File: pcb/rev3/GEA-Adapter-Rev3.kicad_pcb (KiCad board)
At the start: 2 copper layers, 88.7 x 40 mm, 109 parts, among them J1 8P8C, J3 TC2030, J4 USB_C_Receptacle_USB2.0_16P, Q3 CJ3407, Q4 CJ3407, Q5 MMBT3904, SW1 SW_Push, SW2 SW_Push, U10 TPS22810DBVR, U2 ESP32-C3-WROOM-02, U4 74LVC2G07, U5 74LVC2G07_3v3, U6 AP2112K-3.3, U7 USBLC6-2SC6, U8 AP63205WU, U9 TPS22810DBVR

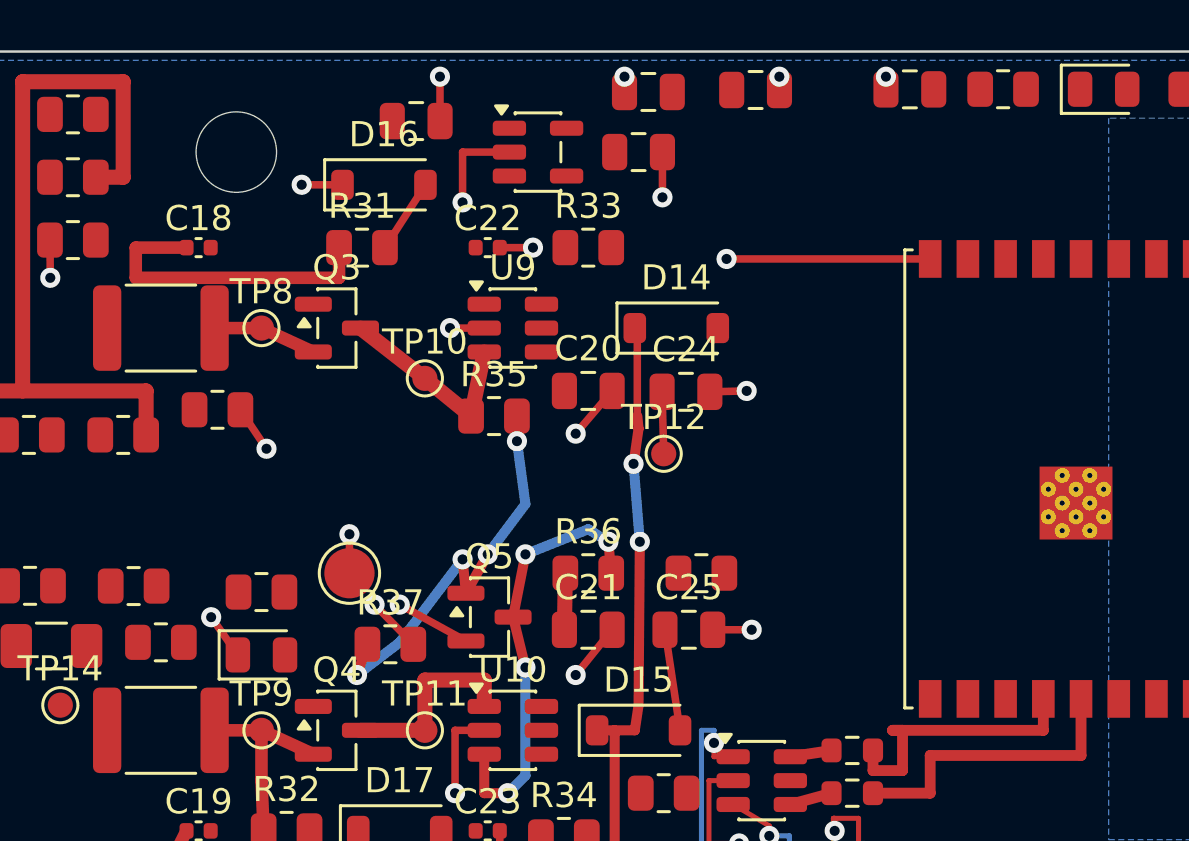
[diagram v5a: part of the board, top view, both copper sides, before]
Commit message: feat(pcb): route rev3a 3v3 branches
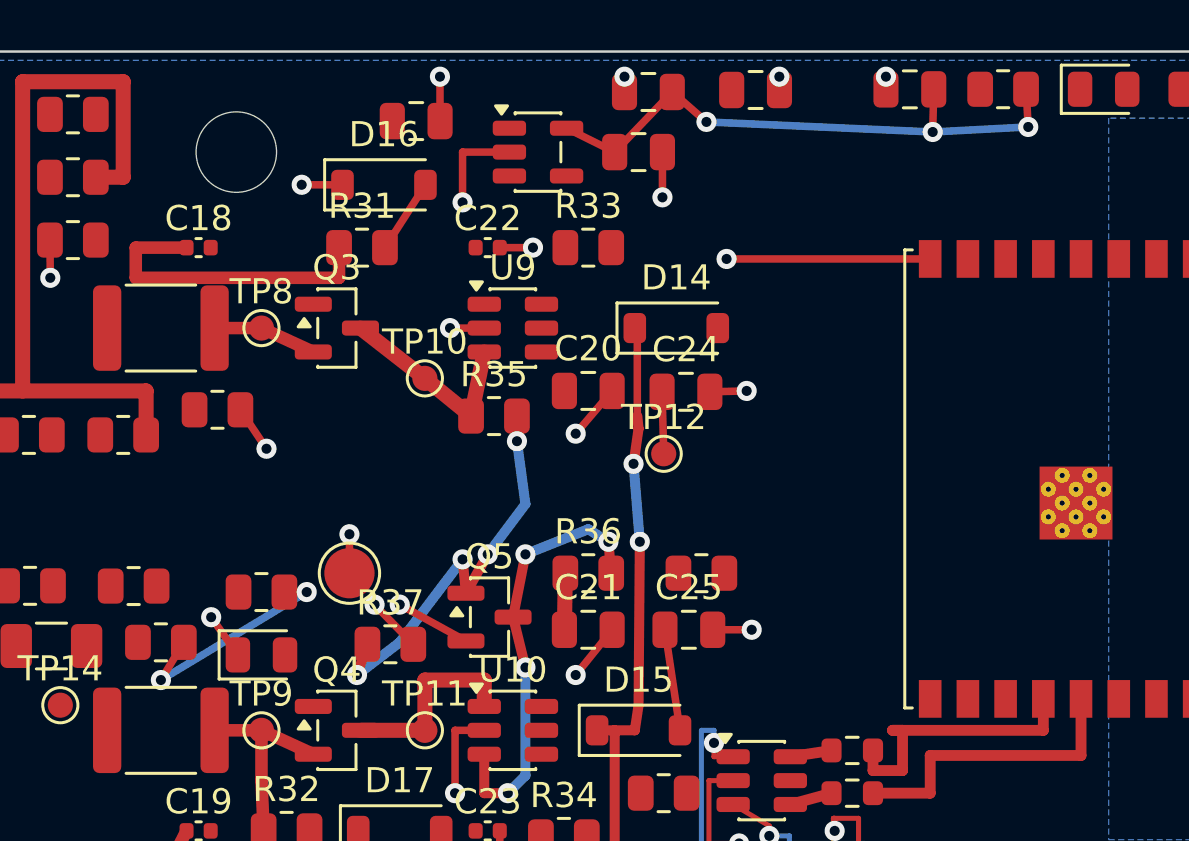
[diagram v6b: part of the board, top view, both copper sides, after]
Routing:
- net +3V3: track 2.17 -> 34.9 mm, vias 0 -> 5
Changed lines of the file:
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@@
+	)
+	(segment
+		(start 79.5 3)
+		(end 79.4125 1.5)
+		(width 0.3)
+		(layer "F.Cu")
+		(net 1)
+	)
+	(segment
+		(start 50.8 21.5)
+		(end 49.9125 21.5)
+		(width 0.3)
+		(layer "F.Cu")
+		(net 1)
+	)
+	(segment
+		(start 65.341108 1.60873)
+		(end 66.7 2.8)
+		(width 0.3)
+		(layer "F.Cu")
+		(net 1)
+	)
+	(segment
+		(start 75.7 3.2)
+		(end 75.741054 1.50506)
+		(width 0.3)
+		(layer "F.Cu")
+		(net 1)
+	)
+	(segment
+		(start 61.1375 3.05)
+		(end 63.05 4)
+		(width 0.3)
+		(layer "F.Cu")
+		(net 1)
+	)
+	(segment
+		(start 45.9125 23.5)
+		(end 45 25)
+		(width 0.3)
+		(layer "F.Cu")
+		(net 1)
+	)
+	(segment
+		(start 63.05 4)
+		(end 65.341108 1.60873)
+		(width 0.3)
+		(layer "F.Cu")
+		(net 1)
 	)
 	(segment
@@
 		(net 1)
 	)
+	(via
+		(at 45 25)
+		(size 0.8)
+		(drill 0.4)
+		(layers "F.Cu" "B.Cu")
+		(net 1)
+	)
+	(via
+		(at 50.8 21.5)
+		(size 0.8)
+		(drill 0.4)
+		(layers "F.Cu" "B.Cu")
+		(net 1)
+	)
+	(via
+		(at 75.7 3.2)
+		(size 0.8)
+		(drill 0.4)
+		(layers "F.Cu" "B.Cu")
+		(net 1)
+	)
+	(via
+		(at 66.7 2.8)
+		(size 0.8)
+		(drill 0.4)
+		(layers "F.Cu" "B.Cu")
+		(net 1)
+	)
+	(via
+		(at 79.5 3)
+		(size 0.8)
+		(drill 0.4)
+		(layers "F.Cu" "B.Cu")
+		(net 1)
+	)
+	(segment
+		(start 45 25)
+		(end 50.8 21.5)
+		(width 0.3)
+		(layer "B.Cu")
+		(net 1)
+	)
+	(segment
+		(start 75.7 3.2)
+		(end 79.5 3)
+		(width 0.3)
+		(layer "B.Cu")
+		(net 1)
+	)
+	(segment
+		(start 66.7 2.8)
+		(end 75.7 3.2)
+		(width 0.3)
+		(layer "B.Cu")
+		(net 1)
+	)

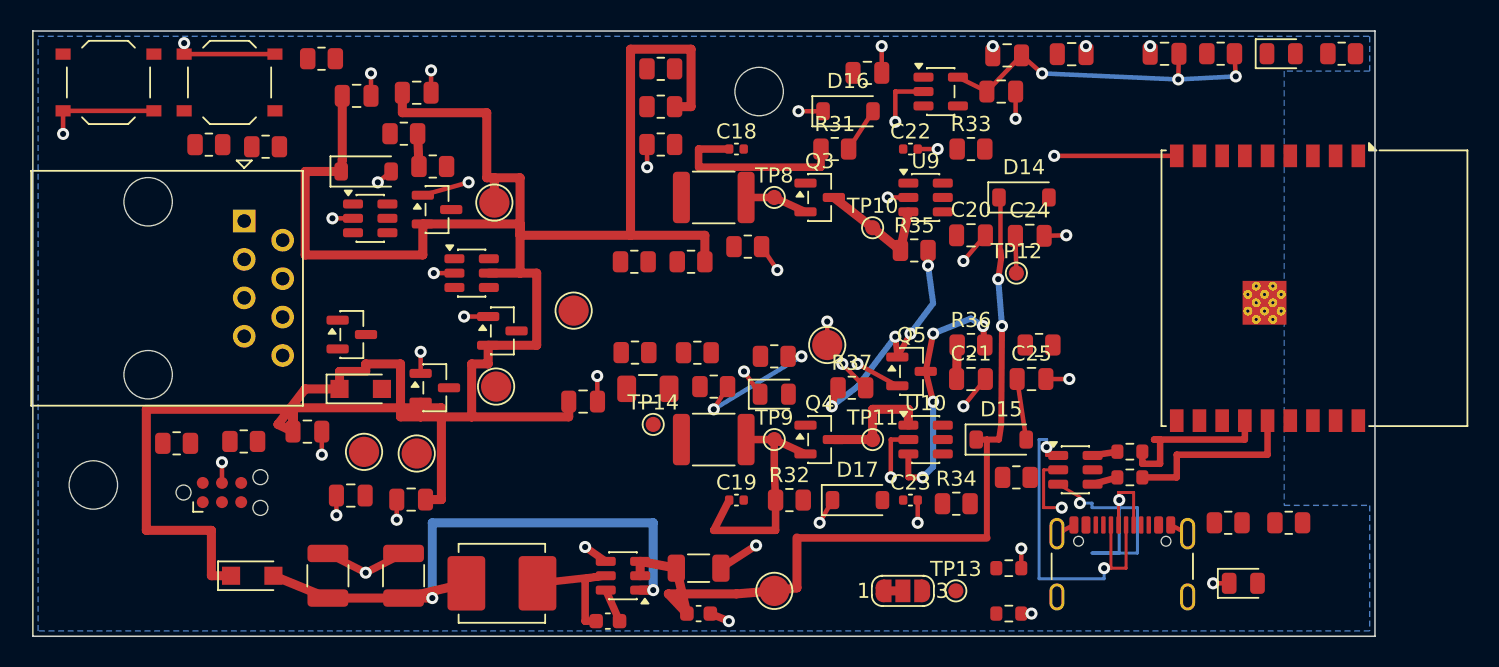
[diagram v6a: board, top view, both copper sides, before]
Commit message: feat(pcb): finish rev3a 5v distribution
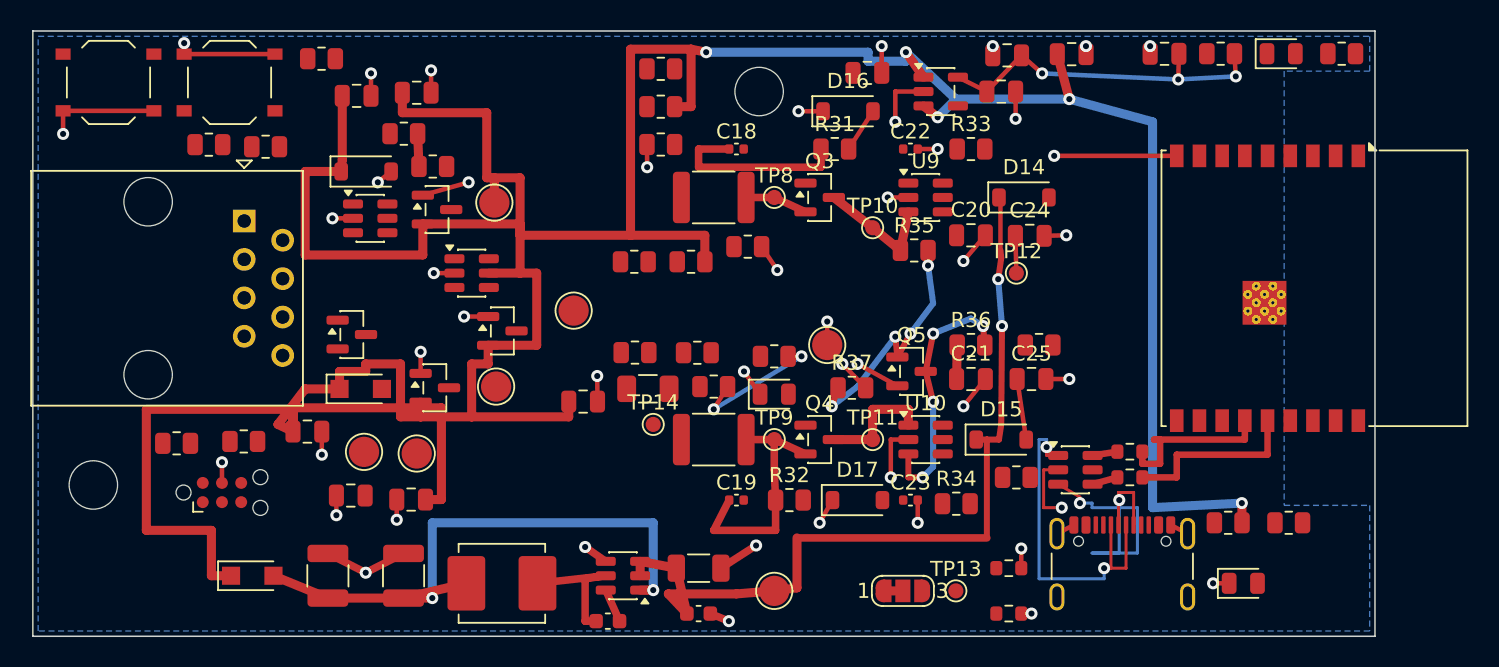
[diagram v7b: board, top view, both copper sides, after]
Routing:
- net +5V: track 178.2 -> 252.1 mm, vias 0 -> 5
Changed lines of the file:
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@@
+	)
+	(segment
+		(start 43.5 1.2)
+		(end 44.5 1.4)
+		(width 0.6)
+		(layer "F.Cu")
+		(net 2)
 	)
 	(segment
@@
 	)
 	(segment
+		(start 57.7 1.4)
+		(end 58.8625 3.05)
+		(width 0.6)
+		(layer "F.Cu")
+		(net 2)
+	)
+	(segment
 		(start 18 14.8)
 		(end 25.7752 14.8)
@@
 	)
 	(segment
+		(start 59.8 5.7)
+		(end 58.8625 4.95)
+		(width 0.6)
+		(layer "F.Cu")
+		(net 2)
+	)
+	(segment
 		(start 25.7752 14.8)
 		(end 25.7752 12.7499)
@@
 	)
 	(segment
+		(start 68.5 4.5)
+		(end 67.7044 1.529956)
+		(width 0.6)
+		(layer "F.Cu")
+		(net 2)
+	)
+	(segment
 		(start 25.6291 25.5)
 		(end 25.6291 24.5271)
@@
 	)
 	(segment
+		(start 79.9 31.2)
+		(end 79.9125 32.5)
+		(width 0.6)
+		(layer "F.Cu")
+		(net 2)
+	)
+	(segment
 		(start 30.092 22)
 		(end 29 22)
@@
 		(net 2)
 	)
+	(via
+		(at 59.8 5.7)
+		(size 0.8)
+		(drill 0.4)
+		(layers "F.Cu" "B.Cu")
+		(net 2)
+	)
+	(via
+		(at 57.7 1.4)
+		(size 0.8)
+		(drill 0.4)
+		(layers "F.Cu" "B.Cu")
+		(net 2)
+	)
+	(via
+		(at 68.5 4.5)
+		(size 0.8)
+		(drill 0.4)
+		(layers "F.Cu" "B.Cu")
+		(net 2)
+	)
+	(via
+		(at 44.5 1.4)
+		(size 0.8)
+		(drill 0.4)
+		(layers "F.Cu" "B.Cu")
+		(net 2)
+	)
+	(via
+		(at 79.9 31.2)
+		(size 0.8)
+		(drill 0.4)
+		(layers "F.Cu" "B.Cu")
+		(net 2)
+	)
+	(segment
+		(start 74 6)
+		(end 74 31.5)
+		(width 0.6)
+		(layer "B.Cu")
+		(net 2)
+	)
+	(segment
+		(start 61 4.5)
+		(end 68.5 4.5)
+		(width 0.6)
+		(layer "B.Cu")
+		(net 2)
+	)
+	(segment
+		(start 55.2 1.4)
+		(end 55.2 2)
+		(width 0.6)
+		(layer "B.Cu")
+		(net 2)
+	)
+	(segment
+		(start 57.7 2)
+		(end 57.7 1.4)
+		(width 0.6)
+		(layer "B.Cu")
+		(net 2)
+	)
+	(segment
+		(start 74 31.5)
+		(end 79.9 31.2)
+		(width 0.6)
+		(layer "B.Cu")
+		(net 2)
+	)
+	(segment
+		(start 59.8 5.7)
+		(end 61 4.5)
+		(width 0.6)
+		(layer "B.Cu")
+		(net 2)
+	)
+	(segment
+		(start 57.7 1.4)
+		(end 61 4.5)
+		(width 0.6)
+		(layer "B.Cu")
+		(net 2)
+	)
+	(segment
+		(start 68.5 4.5)
+		(end 74 6)
+		(width 0.6)
+		(layer "B.Cu")
+		(net 2)
+	)
+	(segment
+		(start 55.2 2)
+		(end 57.7 2)
+		(width 0.6)
+		(layer "B.Cu")
+		(net 2)
+	)
+	(segment
+		(start 44.5 1.4)
+		(end 55.2 1.4)
+		(width 0.6)
+		(layer "B.Cu")
+		(net 2)
+	)

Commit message: feat(pcb): route rev3a secondary transmit
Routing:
- net GEA2_TX: track 0.00 -> 33.8 mm, vias 0 -> 2
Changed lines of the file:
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@@
+	)
+	(segment
+		(start 43.003375 21.261812)
+		(end 43 19.5)
+		(width 0.4)
+		(layer "F.Cu")
+		(net 12)
+	)
+	(segment
+		(start 57.5 37)
+		(end 57.5 35)
+		(width 0.4)
+		(layer "F.Cu")
+		(net 12)
+	)
+	(via
+		(at 43 19.5)
+		(size 0.8)
+		(drill 0.4)
+		(layers "F.Cu" "B.Cu")
+		(net 12)
+	)
+	(via
+		(at 57.5 35)
+		(size 0.8)
+		(drill 0.4)
+		(layers "F.Cu" "B.Cu")
+		(net 12)
+	)
+	(segment
+		(start 43 35)
+		(end 57.5 35)
+		(width 0.4)
+		(layer "B.Cu")
+		(net 12)
+	)
+	(segment
+		(start 43 19.5)
+		(end 43 35)
+		(width 0.4)
+		(layer "B.Cu")
+		(net 12)
 	)
 	(segment
